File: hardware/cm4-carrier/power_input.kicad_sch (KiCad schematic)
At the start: 10 parts, among them J1 USB4110-GF-A, J2 LiPo 3.7V 3000mAh, U1 MCP73831-2ACI/OT

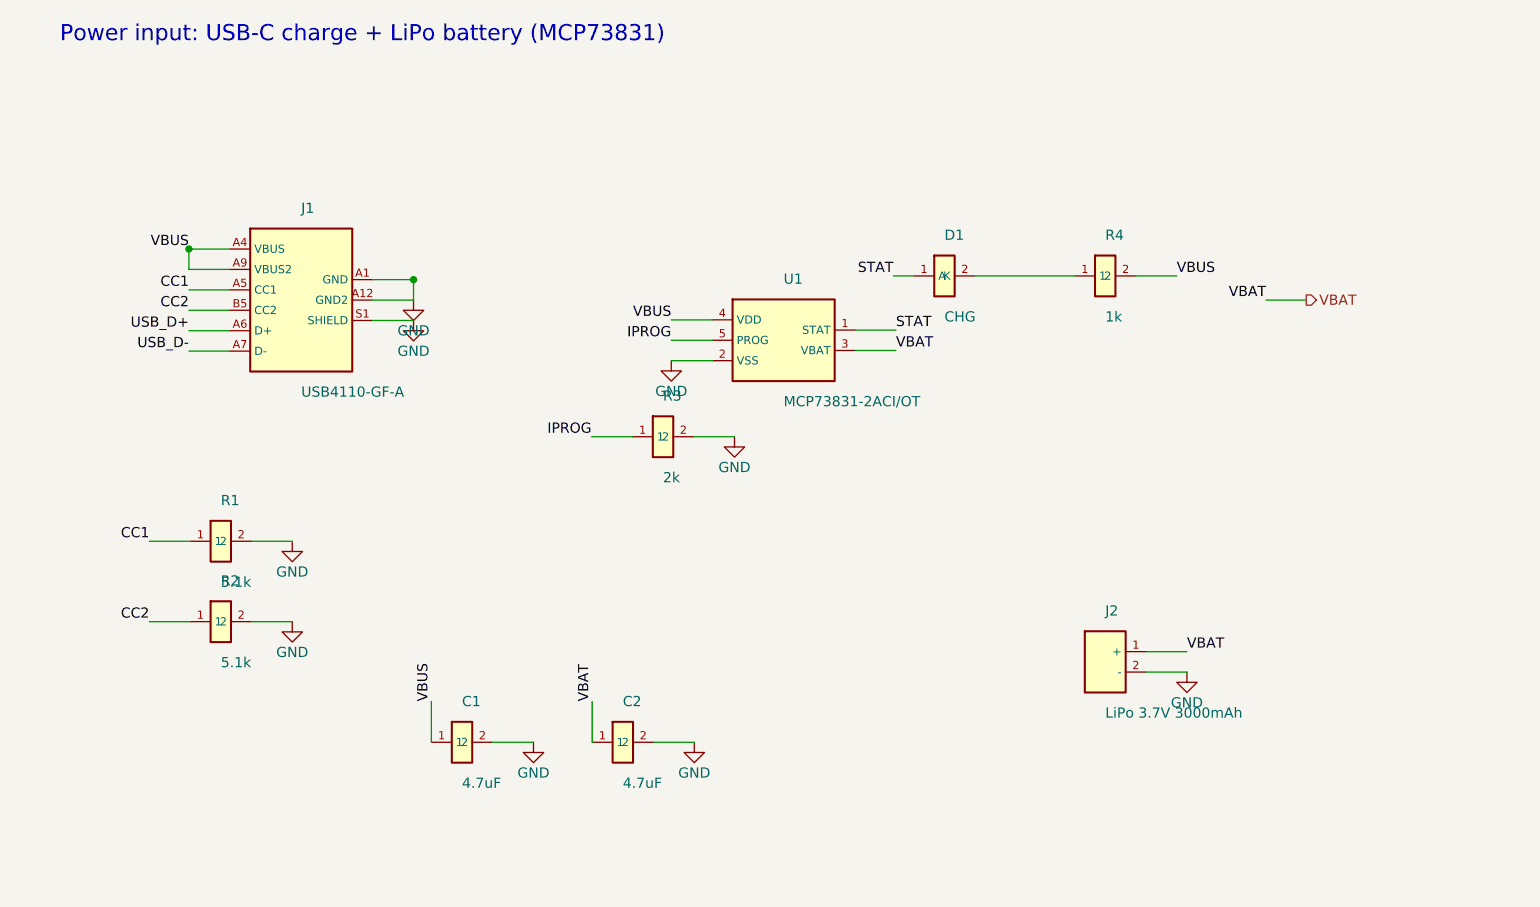
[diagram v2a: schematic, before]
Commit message: Add Dynamic Power Path Management and battery protection
Rework the power architecture to add DPPM and dedicated cell protection.

Power path (DPPM): replace the MCP73831 with a TI BQ24075 USB-friendly
charger whose OUT pin is a separate system rail (SYS). The load now runs
directly from USB when present (system works with a dead/absent battery and
the cell is not needlessly cycled) and falls back to the battery when USB is
removed, while the cell charges from the remaining input budget. Adds ISET,
ILIM and TMR programming resistors, EN1/EN2/CE/SYSOFF strapping, a 10k NTC
on TS for battery-temperature protection, and CHG/PGOOD status LEDs. The
5 V boost regulator now draws from SYS instead of VBAT.

Battery protection: new battery_protection.kicad_sch sub-sheet with an
AP9101CK6 1-cell protection controller (DW01A-class) driving an FS8205A dual
N-MOSFET in the cell's negative line — over-charge, over-discharge,
over-current and short-circuit cutoff. The raw JST cell connector moves here;
its protected terminals feed VBAT/GND to the rest of the board.

Pinouts for BQ24075 and AP9101CK6 were taken from KiCad's Battery_Management
library. Root sheet gains the Battery Protection box and the SYS net; all
hierarchical labels match their sheet pins and reference designators are
globally unique. README/BOM updated. No format change (KiCad 10, 20260306).

Co-Authored-By: Claude Opus 4.8 <noreply@anthropic.com>
Claude-Session: https://claude.ai/code/session_015B7X7FE461jFSRaiTFdnFt
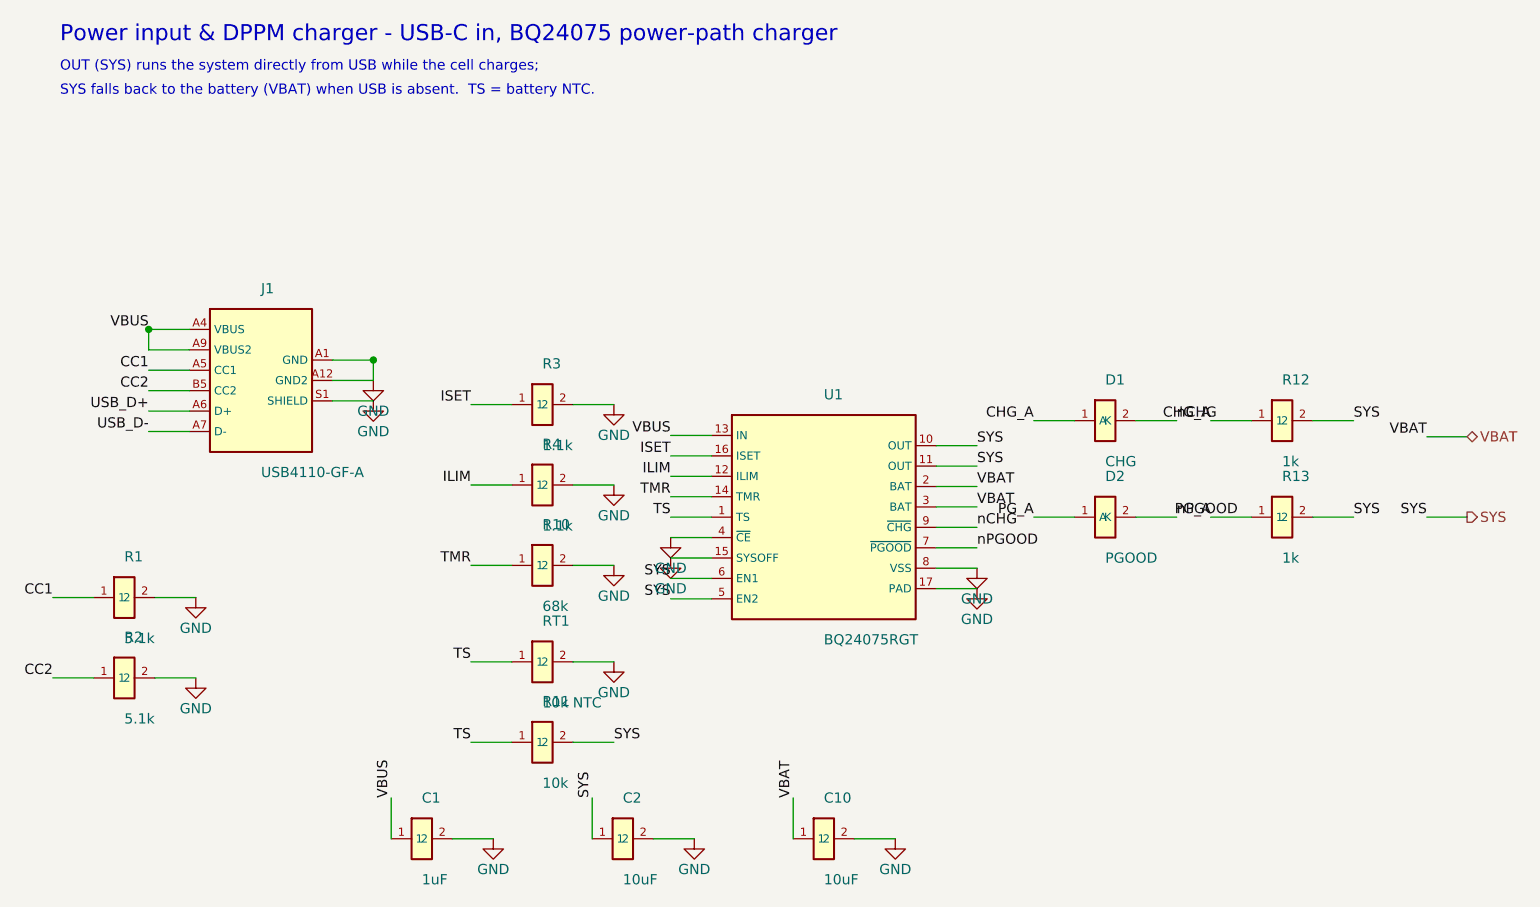
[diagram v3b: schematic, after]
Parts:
- removed J2: LiPo 3.7V 3000mAh, Connector_JST:JST_GH_SM02B-GHS-TB_1x02-1MP_P1.25mm_Horizontal, symbol carrier:Conn_01x02
- removed U1: MCP73831-2ACI/OT, Package_TO_SOT_SMD:SOT-23-5, symbol carrier:MCP73831
- added C10: 10uF, Capacitor_SMD:C_0805_2012Metric, symbol carrier:C
- added D2: PGOOD, LED_SMD:LED_0603_1608Metric, symbol carrier:LED
- added R10: 68k, Resistor_SMD:R_0402_1005Metric, symbol carrier:R
- added R11: 10k, Resistor_SMD:R_0402_1005Metric, symbol carrier:R
- added R12, R13: 1k, Resistor_SMD:R_0402_1005Metric, symbol carrier:R
- added RT1: 10k NTC, Resistor_SMD:R_0603_1608Metric, symbol carrier:R
- added U1: BQ24075RGT, Package_DFN_QFN:VQFN-16-1EP_3x3mm_P0.5mm_EP1.7x1.7mm, symbol carrier:BQ24075
- C1: value 4.7uF -> 1uF
- C2: value 4.7uF -> 10uF; footprint Capacitor_SMD:C_0603_1608Metric -> Capacitor_SMD:C_0805_2012Metric
- R3: value 2k -> 1.1k
- R4: value 1k -> 1.1k
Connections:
- net GND: now also R4.2, C10.2, R10.2, RT1.2, U1.15 (SYSOFF), U1.17 (PAD), U1.4 (~{CE}), U1.8 (VSS)
- net VBAT: now also C10.1, U1.2 (BAT), U1.3 (BAT); no longer C2.1
- net VBUS: now also U1.13 (IN); no longer R4.2
- net ILIM: now reaches R4.1
- net ILIM: now also U1.12 (ILIM); no longer D1.2 (K)
- net IPROG renamed ISET
- net ISET: now also U1.16 (ISET)
- net STAT renamed CHG_A
- net CHG_A: now also R12.1
- new net PG_A: D2.1 (A), R13.1
- new net SYS: C2.1, R11.2, R12.2, R13.2, U1.10 (OUT), U1.11 (OUT), U1.5 (EN2), U1.6 (EN1)
- new net TMR: R10.1, U1.14 (TMR)
- new net TS: R11.1, RT1.1, U1.1 (TS)
- new net nCHG: D1.2 (K), U1.9 (~{CHG})
- new net nPGOOD: D2.2 (K), U1.7 (~{PGOOD})
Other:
- note added: "OUT (SYS) runs the system directly from USB while the cell charges;"
- note added: "Power input & DPPM charger - USB-C in, BQ24075 power-path charger"
- note added: "SYS falls back to the battery (VBAT) when USB is absent. TS = battery NTC."
- note removed: "Power input: USB-C charge + LiPo battery (MCP73831)"
